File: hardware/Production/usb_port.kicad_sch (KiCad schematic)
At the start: 95 parts, among them J401 TYPE-C 16PCB1.6 IP68, Q401 SiZ240DT, Q402 SiZ240DT, U401 TPS25751DREFR, U402 M24512-DFMC6TG, U403 BQ25756RRVR, U404 TPS62933DRLR, U405 TPD6S300RUKR

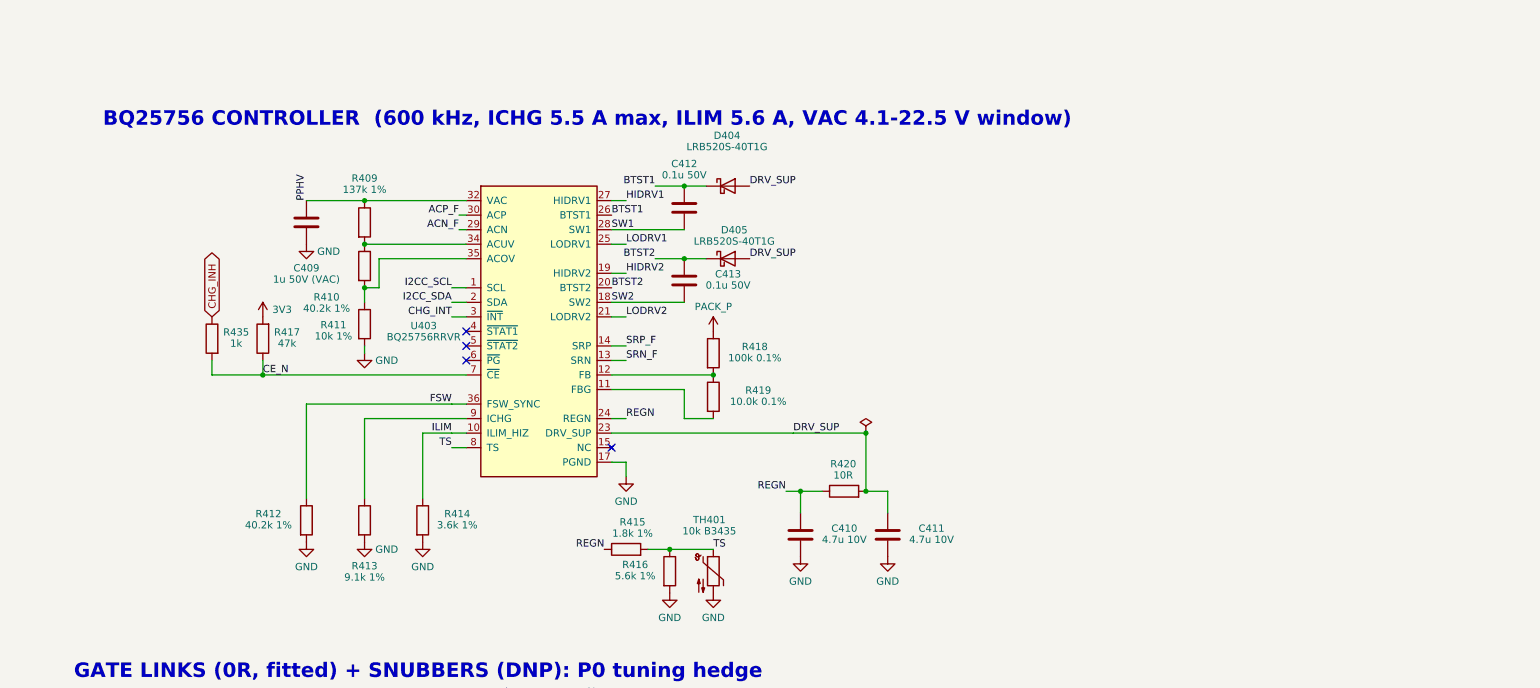
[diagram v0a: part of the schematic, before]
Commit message: FEB 21700G 6500 mAh cells replace the EVE 58E (93.6 Wh)
- Mechanical: cells designed to 21.85 x 71.1 mm; pitch 23.25 mm; tray 0.7 mm
  wider and 0.35 mm deeper, same length. Board outline unchanged (guide line
  held at the 58E value); extra cell length taken from the floor zone
  (SB_PAD_T 4.6 -> 4.3). Five bottom slots move 0.30 mm, PACK/Kelvin pairs
  0.18 mm outward; CELL1/3 unchanged. Frame-bar check now measures bearing
  height; tail kink +0.35 mm. Cells 75 g: pack ~387 g modelled. All outputs
  re-rendered, label 6.5 Ah / 93.6 Wh.
- Schematic: R413/R513 (ICHG) 9.1k -> 11.8k (C93752): hardware charge
  ceiling 4.07-4.45 A, under the FEB's 4.55 A maximum.
- Docs: FEB datasheet notes, firmware charge and thermal policy, P0 assembly
  slot table and cells, gauge setup (capacity, temperature ranges,
  protections, chemistry), README, mechanical design, production README.
- Not applied: Monolith.kicad_pcb (slots, R413/R513 values), pending the
  in-progress layout.

Co-Authored-By: Claude Opus 5.5 <noreply@anthropic.com>
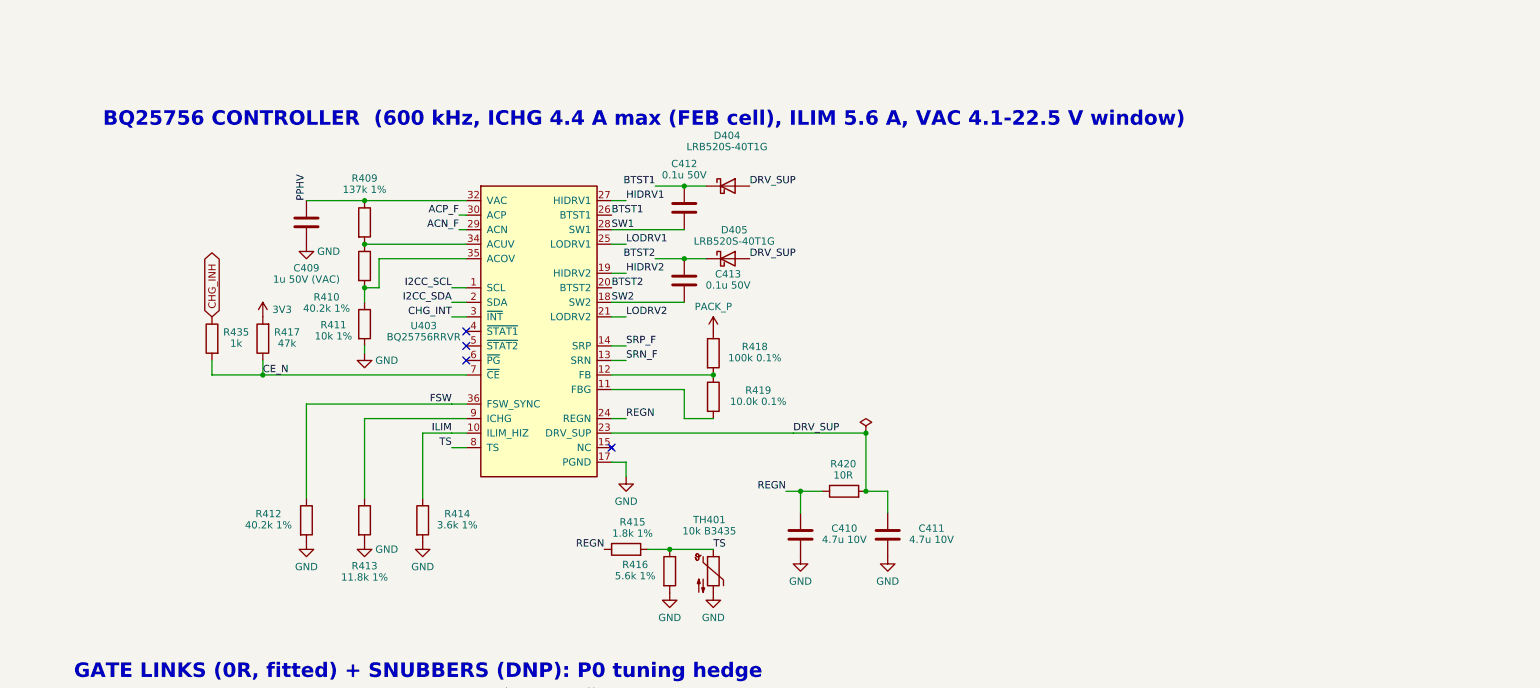
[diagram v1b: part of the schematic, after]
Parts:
- R413: value 9.1k 1% -> 11.8k 1%; LCSC C25926 -> C93752; MPN 0402WGF9101TCE -> 0402WGF1182TCE; Notes ICHG hardware ceiling 50/9.1 = 5.5 A per port (5.3-5.8 A ov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 -> ICHG hardware ceiling 50/11.8 = 4.24 A per port (4.07-4.45 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
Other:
- note added: "BQ25756 CONTROLLER (600 kHz, ICHG 4.4 A max (FEB cell), ILIM 5.6 A, VAC 4.1-22.5 V window)"
- note removed: "BQ25756 CONTROLLER (600 kHz, ICHG 5.5 A max, ILIM 5.6 A, VAC 4.1-22.5 V window)"
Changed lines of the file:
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@@
 		)
 	)
-	(text "BQ25756 CONTROLLER  (600 kHz, ICHG 5.5 A max, ILIM 5.6 A, VAC 4.1-22.5 V window)"
+	(text "BQ25756 CONTROLLER  (600 kHz, ICHG 4.4 A max (FEB cell), ILIM 5.6 A, VAC 4.1-22.5 V window)"
 		(exclude_from_sim no)
 		(at 304.8 167.64 0)
@@
 			)
 		)
-		(property "Value" "9.1k 1%"
+		(property "Value" "11.8k 1%"
 			(at 350.52 246.17 0)
 			(show_name no)
@@
 			)
 		)
-		(property "Notes" "ICHG hardware ceiling 50/9.1 = 5.5 A per port (5.3-5.8 A over K_ICHG and 1 %): one port can charge at about 1C. Firmware keeps the sum of both ports at 5.6 A max (TPS25751 config default ICHG_REG 2.8 A; MCU raises the only charging port). EN_CHG_BIT_RESET_BEHAVIOR = 0 so a watchdog expiry stops charging instead of falling back to this pin"
+		(property "Notes" "ICHG hardware ceiling 50/11.8 = 4.24 A per port (4.07-4.45 A over K_ICHG and 1 %), under the FEB 21700G cell's 4.55 A charge maximum (2026-10-21; was 9.1k for the EVE 58E). Firmware keeps the sum of both ports at 4.55 A max and follows the cell-temperature charge ramp (docs/firmware/charge-and-thermal-policy.md; TPS25751 config default ICHG_REG 2.8 A; MCU raises the only charging port). EN_CHG_BIT_RESET_BEHAVIOR = 0 so a watchdog expiry stops charging instead of falling back to this pin"
 			(at 0 0 0)
 			(hide yes)
@@
 			)
 		)
-		(property "LCSC" "C25926"
+		(property "LCSC" "C93752"
 			(at 350.52 236.22 0)
 			(hide yes)
@@
 			)
 		)
-		(property "MPN" "0402WGF9101TCE"
+		(property "MPN" "0402WGF1182TCE"
 			(at 350.52 236.22 0)
 			(hide yes)

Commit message: Production board: tail slots, 1N/4P Kelvin nets, carrier peg holes, cup keep-outs
Schematic (make_production.py, regenerated):
- J108-J112 become plated slots for the nickel tails; J115 (1N) and J116 (4P)
  are the Kelvin fingers on new nets CELL_1N / CELL_4P (SLUA660 2.3-2.4).
  CELL_1N: gauge VSS star, U102 VSS, decoupling, NTC returns. CELL_4P: VC4,
  U102 V4/VDD, D101. Shunt, SRP and Q104 stay on CELL_N; F102 on CELL_P_RAW.
- H101-H104: cover standoffs -> 2.2 mm NPTH carrier peg holes.
- R413/R513 11.8k and the ICHG heading now come from the generator.
- Symbol uuids are kept across regens so Update PCB keeps placed parts.
- check_netlist accepts "new NAME" net moves; tidy notes updated.

Board: cup keep-outs (rails split at the filler, gap filler, tail runs,
vent, antenna, top stops), footprints swapped and nets applied from the
schematic (checked pad by pad), slots and pegs placed and locked.

make_board.py: --keepouts writes zones as text (KiCad 10 python can't build
outlines), --mech replaces --standoffs and keeps the .kicad_pro.
monolith_shell.py holds the cup's board-facing values (CUP_*, cup_rails).
Docs: README sections, p0-assembly solder order and Kelvin wording.

Co-Authored-By: Claude Opus 5.5 <noreply@anthropic.com>
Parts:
- removed unit 2 of Q401
- removed unit 1 of Q402
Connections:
- net BAT_SNS_P: now also Q402.2 (D1), Q402.3 (D1), Q402.4 (D1)
- net GND: now also Q401.5 (S2), Q401.6 (S2), Q401.7 (S2)
- net HG2: now also Q402.1 (G1)
- net LG1: now also Q401.8 (G2)
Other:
- moved on the sheet: Q401B, Q402A

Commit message: P0 schematic: protection FETs, 9 V gate drive and inductor loss cuts
The three board-side loss cuts approved on 2026-10-23 were in the spec
but never drawn. Now in the production schematic (port 1 refs):

- Cut 1: Q101/Q102 AGM404AP1 -> Infineon BSC007N04LS6 (C534274) on a
  5 x 6 footprint, KiCad's PG-TDSON-8 with the drain leads numbered 5-8
- Cut 2: 9 V DRV_SUP per port. U406 TPS7A4101 (C111739) from PACK_P,
  ~9.6 V via R452/R453, ORed onto DRV_SUP by D411; D410 replaces R420
  (REGN -> DRV_SUP) so the standard drive and dead-pack charging stay.
  EN = REGN via R454, held low by Q409 unless TPS25751 GPIO6 (DRV9_OFF,
  freed from the GND rail) is low: off by default, GPsl on, GPsh off.
  C411 -> 4.7u 25V 0805.
- Cut 3: L401 Coilcraft XGL7030-332 on the APS0730 pads, R412 49.9k
  (~500 kHz)

make_production.py builds all of it (add_gate_drive, free_gpio6,
tdson_footprint, tps7a4101.py); the committed sheets were updated with
the same functions since KiCad isn't available here. A script net diff
shows only the intended changes, and a regenerated usb/gauge sheet
matches. check_netlist.py knows the new nets. ERC and Update PCB from
Schematic are still to run in KiCad.

Co-Authored-By: Claude Opus 5.5 <noreply@anthropic.com>
Claude-Session: https://claude.ai/code/session_01LzE9uyZaPiG6jLirJVJbfw
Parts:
- added C457: 1u 50V, Capacitor_SMD:C_0603_1608Metric, symbol Device:C
- added C458: 22u 25V, Capacitor_SMD:C_0805_2012Metric, symbol Device:C
- added D411: LRB520S-40T1G, Diode_SMD:D_SOD-523, symbol Device:D_Schottky
- added Q409: AO3400A, Package_TO_SOT_SMD:SOT-23, symbol Transistor_FET:Q_NMOS_GSD
- added R452: 40.2k 1%, Resistor_SMD:R_0402_1005Metric, symbol Device:R
- added R453: 5.6k 1%, Resistor_SMD:R_0402_1005Metric, symbol Device:R
- added R454, R455: 100k, Resistor_SMD:R_0201_0603Metric, symbol Device:R
- added U406: TPS7A4101DGNR, Package_SO:HVSSOP-8-1EP_3x3mm_P0.65mm_EP1.57x1.89mm, symbol MonolithDev:TPS7A4101
- C411: value 4.7u 10V -> 4.7u 25V; footprint Capacitor_SMD:C_0402_1005Metric -> Capacitor_SMD:C_0805_2012Metric; LCSC C23733 -> C1779; MPN CL05A475MP5NRNC -> CL21A475KAQNNNE
- D410: renamed from R420; value 10R -> LRB520S-40T1G; footprint Resistor_SMD:R_0402_1005Metric -> Diode_SMD:D_SOD-523; symbol Device:R -> Device:D_Schottky; LCSC C25077 -> C132124; MPN 0402WGF100JTCE -> LRB520S-40T1G
- L401: value 2.2u -> 3.3u; LCSC C49261221 -> (none); MPN APS0730M2R2F (Coilank) -> XGL7030-332MEC (Coilcraft); Notes Cost-down 2026-10-14 (was Coilcraft XAL7030-222): 2.2 uH, D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 -> Coilcraft XGL7030-332MEC, 3.3 uH, 10.4/12.5 mOhm typ/max, >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
- R412: value 40.2k 1% -> 49.9k 1%; LCSC C423536 -> (none); MPN 0201WMF4022TEE -> 0201WMF4992TEE; Notes FSW ~600 kHz; the oscillator is +/-15 %, so 1 % is plenty -> FSW ~500 kHz (loss cut 3, with L401 XGL7030-332); the oscil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
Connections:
- net DRV_SUP: now also D410.1 (K), D411.1 (K); no longer D410.2
- net GND: now also C457.2, C458.2, Q409.2 (S), R453.2, U406.4 (GND), U406.9 (GND); no longer U401.37 (GPIO6)
- net LDO_3V3: now also R455.1
- net PACK_P: now also C457.1, U406.8 (IN)
- net REGN: now also D410.2 (A), R454.2; no longer D410.1
- new net: R452.2, R453.1, U406.2 (FB)
- new net: C458.1, D411.2 (A), R452.1, U406.1 (OUT)
- new net: Q409.3 (D), R454.1, U406.5 (EN)
- new net DRV9_OFF: Q409.1 (G), R455.2, U401.37 (GPIO6)
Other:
- note added: "9 V GATE DRIVE (DRV_SUP): fitted, off by default (loss cut 2)"
- note added: "BQ25756 CONTROLLER (500 kHz, ICHG 4.4 A max (FEB cell), ILIM 5.6 A, VAC 4.1-22.5 V window)"
- note added: "NOTES (this sheet is used twice: USB Port 1 = 4xx, USB Port 2 = 5xx) 1. Address straps are on the root sheet: port 1 ADCIN1 = LDO_3V3, ADCIN2 = GND (0x20); port 2 ADCIN1 = ADCIN2 = GND (0x21). Both are SafeMode (TPS25751 table 8-6). 2. Unused TPS25751 GPIOs (0, 1, 2, 4, 5, 7, 11) tied to GND per datasheet (KiCad ERC flags this; expected). Never configure them as outputs. GPIO6 = DRV9_OFF, the 9 V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"
- note added: "U406 TPS7A4101 from PACK_P sets ~9.6 V (R452/R453); D411 ORs it onto DRV_SUP (~9.3 V). D410 (was R420 10R) feeds REGN - VF while U406 is off: TI's standard drive, so a dead pack still charges. EN = REGN via R454, held low by Q409 unless TPS25751 GPIO6 (DRV9_OFF) is low: GPIO6 Hi-Z or high = off. Configure GPIO6 as an output, initial high; 'GPsl' on, 'GPsh' off. Firmware: on only while this conver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"
- note removed: "BQ25756 CONTROLLER (600 kHz, ICHG 4.4 A max (FEB cell), ILIM 5.6 A, VAC 4.1-22.5 V window)"
- note removed: "NOTES (this sheet is used twice: USB Port 1 = 4xx, USB Port 2 = 5xx) 1. Address straps are on the root sheet: port 1 ADCIN1 = LDO_3V3, ADCIN2 = GND (0x20); port 2 ADCIN1 = ADCIN2 = GND (0x21). Both are SafeMode (TPS25751 table 8-6). 2. Unused TPS25751 GPIOs (0, 1, 2, 4-7, 11) tied to GND per datasheet (KiCad ERC flags this; expected). Never configure them as outputs. 3. CC is protected by U405 (T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"
